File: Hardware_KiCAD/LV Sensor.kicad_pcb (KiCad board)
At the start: 2 copper layers, 98.5 x 50 mm, 97 parts, among them IC1 MCP2517FDT-H_SL, IC2 MC7805CD2TR4G, IC3 TLV74133PDBVR, IC4 TLV74125PDBVR, IC5 MSPM0C1104SDGS20R, IC6 ISO6721BDR, IC7 ISO6721BDR, J1 Screw_Terminal_01x02, J16 USB_B_Micro, J2 Screw_Terminal_01x02, J3 Screw_Terminal_01x02, J4 Screw_Terminal_01x02, J5 Screw_Terminal_01x02, J6 43650-0401, SW1 SW_Push, U0 AP63205WU-7, U10 MCP3204-CI/P, U3 FT231XS-R, U7 ADS114S06BIPBSR, U8 LM2662MX/NOPB, U9 ATA6561-GAQW-N, Y1 830017146

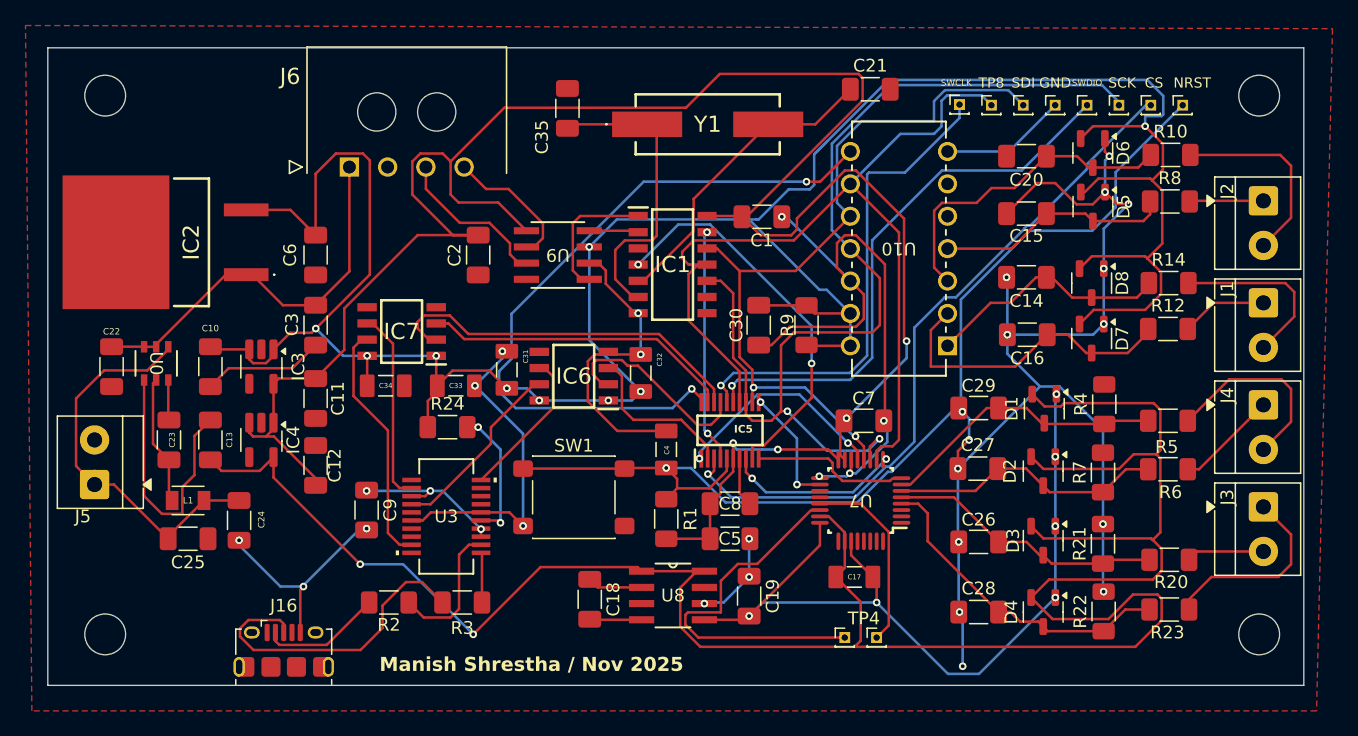
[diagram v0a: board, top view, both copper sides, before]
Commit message: Fixed Layout issues
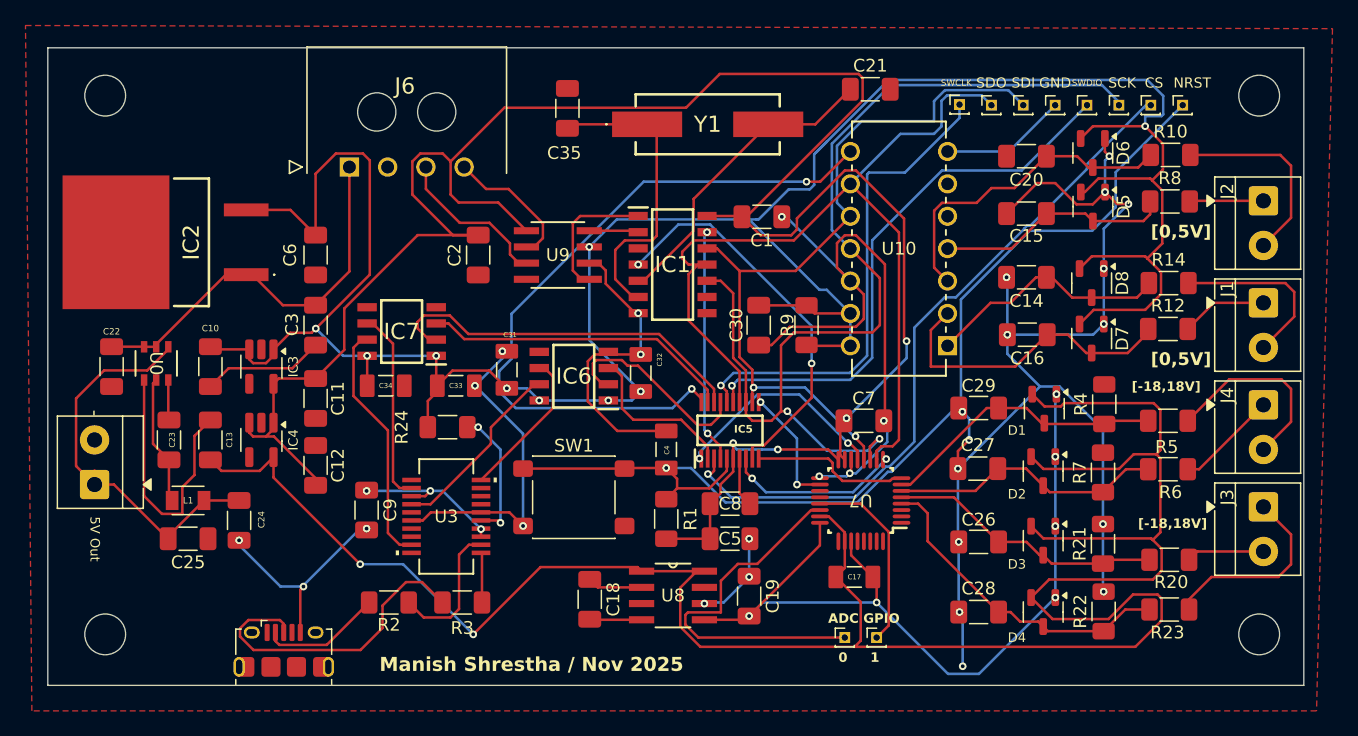
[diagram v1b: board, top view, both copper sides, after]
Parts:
- ADC GPIO: renamed from TP4
- renumbered TP8 to SDO
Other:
- board text added: "-"
- board text added: "0"
- board text added: "1"
- board text added: "5V Out"
- board text added: "[-18,18V]"
- board text added: "[0,5V]"
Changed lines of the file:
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@@
 		(tags "SOT TO_SOT_SMD")
 		(property "Reference" "D3"
-			(at 0 2.3625 90)
+			(at 1.85 2.0625 0)
 			(layer "F.SilkS")
 			(effects
 				(font
-					(size 1 1)
-					(thickness 0.15)
+					(size 0.75 0.75)
+					(thickness 0.09375)
 				)
 			)
@@
 		(tags "SOT TO_SOT_SMD")
 		(property "Reference" "D2"
-			(at 0 2.6125 90)
+			(at 1.8 2.0625 180)
 			(layer "F.SilkS")
 			(effects
 				(font
-					(size 1 1)
-					(thickness 0.15)
+					(size 0.75 0.75)
+					(thickness 0.09375)
 				)
 			)
@@
 		(tags "THT terminal block Metz Connect Type059_RT06302HBWC pitch 3.5mm size 7x6.5mm drill 1.2mm pad 2.3mm")
 		(property "Reference" "J5"
-			(at -2.5 -0.9175 180)
+			(at 6.25 -1.9175 0)
 			(layer "F.SilkS")
+			(hide yes)
 			(effects
 				(font
@@
 		(tags "ATA6561-GAQW-N ")
 		(property "Reference" "U9"
-			(at 0 0 180)
+			(at 0 0 0)
 			(unlocked yes)
 			(layer "F.SilkS")
@@
 		(tags "SOT TO_SOT_SMD")
 		(property "Reference" "D4"
-			(at 0 2.5 90)
+			(at 2 2.0625 0)
 			(layer "F.SilkS")
 			(effects
 				(font
-					(size 1 1)
-					(thickness 0.15)
+					(size 0.75 0.75)
+					(thickness 0.09375)
 				)
 			)
@@
 			(at 0 -3.5 0)
 			(layer "F.SilkS")
+			(hide yes)
 			(effects
 				(font
@@
 		(descr "Through hole straight pin header, 1x01, 1.00mm pitch, single row")
 		(tags "Through hole pin header THT 1x01 1.00mm single row")
-		(property "Reference" "TP4"
+		(property "Reference" "ADC GPIO"
 			(at -1 -1.5 0)
 			(layer "F.SilkS")
 			(effects
 				(font
-					(size 1 1)
+					(size 0.75 0.75)
 					(thickness 0.15)
+					(bold yes)
 				)
 			)
@@
 		(tags "resistor handsolder")
 		(property "Reference" "R24"
-			(at 0 -1.83 0)
+			(at -3.6 0 90)
 			(layer "F.SilkS")
 			(effects
@@
 		(tags "capacitor handsolder")
 		(property "Reference" "C12"
-			(at 0 1.5 90)
+			(at 0 1.75 90)
 			(layer "F.SilkS")
 			(effects
@@
 		(at 166 75 -90)
 		(property "Reference" "C31"
-			(at -1.04 -1.48 90)
+			(at -2.75 -0.25 180)
 			(layer "F.SilkS")
 			(effects
@@
 			(effects
 				(font
-					(size 1 1)
-					(thickness 0.15)
+					(size 0.75 0.75)
+					(thickness 0.09375)
 				)
 			)
@@
 		(tags "capacitor handsolder")
 		(property "Reference" "C35"
-			(at -2.25 -2 90)
+			(at -3.5 -0.25 180)
 			(layer "F.SilkS")
 			(effects
@@
 		(tags "SOT-23-5 hand-soldering")
 		(property "Reference" "IC3"
-			(at 0 -2.9 90)
+			(at 0 -2.5 90)
 			(layer "F.SilkS")
 			(effects
 				(font
-					(size 1 1)
-					(thickness 0.15)
+					(size 0.75 0.75)
+					(thickness 0.09375)
 				)
 			)
@@
 		(tags "SOT TO_SOT_SMD")
 		(property "Reference" "D1"
-			(at 0 2.5625 90)
+			(at 1.7 2.15 0)
 			(layer "F.SilkS")
 			(effects
 				(font
-					(size 1 1)
-					(thickness 0.15)
+					(size 0.75 0.75)
+					(thickness 0.09375)
 				)
 			)
@@
 		(descr "Through hole straight pin header, 1x01, 1.00mm pitch, single row")
 		(tags "Through hole pin header THT 1x01 1.00mm single row")
-		(property "Reference" "TP8"
+		(property "Reference" "SDO"
 			(at 0 -1.75 0)
 			(layer "F.SilkS")
@@
 		(tags "MCP3204-CI/P ")
 		(property "Reference" "U10"
-			(at 3.81 7.62 180)
+			(at 3.81 7.62 0)
 			(unlocked yes)
 			(layer "F.SilkS")
@@
 		(tags "Connector")
 		(property "Reference" "J6"
-			(at 4.65 7.1004 0)
+			(at -4.35 6.3504 0)
 			(layer "F.SilkS")
 			(effects
@@
 		)
 	)
+	(gr_text "[0,5V]"
+		(at 216.5 64.75 0)
+		(layer "F.SilkS")
+		(effects
+			(font
+				(size 1 1)
+				(thickness 0.2)
+				(bold yes)
+			)
+			(justify left bottom)
+		)
+	)
+	(gr_text "[-18,18V]"
+		(at 215 76.75 0)
+		(layer "F.SilkS")
+		(effects
+			(font
+				(size 0.75 0.75)
+				(thickness 0.15)
+				(bold yes)
+			)
+			(justify left bottom)
+		)
+	)
+	(gr_text "5V Out"
+		(at 133.25 86.5 270)
+		(layer "F.SilkS")
+		(effects
+			(font
+				(size 0.75 0.75)
+				(thickness 0.09375)
+			)
+			(justify left bottom)
+		)
+	)
+	(gr_text "[-18,18V]"
+		(at 215.5 87.5 0)
+		(layer "F.SilkS")
+		(effects
+			(font
+				(size 0.75 0.75)
+				(thickness 0.15)
+				(bold yes)
+			)
+			(justify left bottom)
+		)
+	)
 	(gr_text "NRST"
 		(at 219.75 52.5 0)
@@
 		)
 	)
+	(gr_text "[0,5V]"
+		(at 216.5 74.75 0)
+		(layer "F.SilkS")
+		(effects
+			(font
+				(size 1 1)
+				(thickness 0.2)
+				(bold yes)
+			)
+			(justify left bottom)
+		)
+	)
 	(gr_text "SWDIO"
 		(at 211.5 52.5 0)
@@
 		)
 	)
+	(gr_text "1"
+		(at 194.5 98 0)
+		(layer "F.SilkS")
+		(effects
+			(font
+				(size 0.75 0.75)
+				(thickness 0.15)
+				(bold yes)
+			)
+			(justify left bottom)
+		)
+	)
 	(gr_text "SWCLK"
 		(at 201.25 52.5 0)
@@
 		)
 	)
+	(gr_text "0"
+		(at 192 98 0)
+		(layer "F.SilkS")
+		(effects
+			(font
+				(size 0.75 0.75)
+				(thickness 0.15)
+				(bold yes)
+			)
+			(justify left bottom)
+		)
+	)
 	(gr_text "SCK"
 		(at 214.25 52.5 0)
@@
 		)
 	)
+	(gr_text "-"
+		(at 134.1175 78.63 90)
+		(layer "F.SilkS")
+		(effects
+			(font
+				(size 1 1)
+				(thickness 0.1)
+			)
+			(justify left bottom)
+		)
+	)
